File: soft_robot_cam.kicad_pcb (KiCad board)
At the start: 4 copper layers, 134.7 x 96.5 mm, 122 parts, among them J1 Conn_01x24_Socket, J1 Connector, J10 Screw_Terminal_01x02, J2 Conn_01x06, J2 Screw_Terminal_01x02, J3 Conn_01x03, J3 Screw_Terminal_01x02, J4 Conn_01x05_Pin, J6 Screw_Terminal_01x02, J7 Screw_Terminal_01x02, J8 Conn_01x24_Socket, J9 Screw_Terminal_01x02, Q1 S8050, Q2 S8050, Q3 AO3401A, SW1 reset, SW2 SW_DPST_x2, SW4 SW_DIP_x02, U1 DRV8872DDA, U12 XC6206P282MR, U13 XC6206P122MR, U14 SY8113IADC, U2 DRV8872DDA, U3 MPU6500, U4 AP2112K-1.2, U4 DRV8874PWPR, U5 3.3v, U5 DRV8874PWPR, U6 ESP32-WROVER-E, U7 TC2014-2.8VxCTTR, U9 ESP32-S3-WROOM-1-N16R8

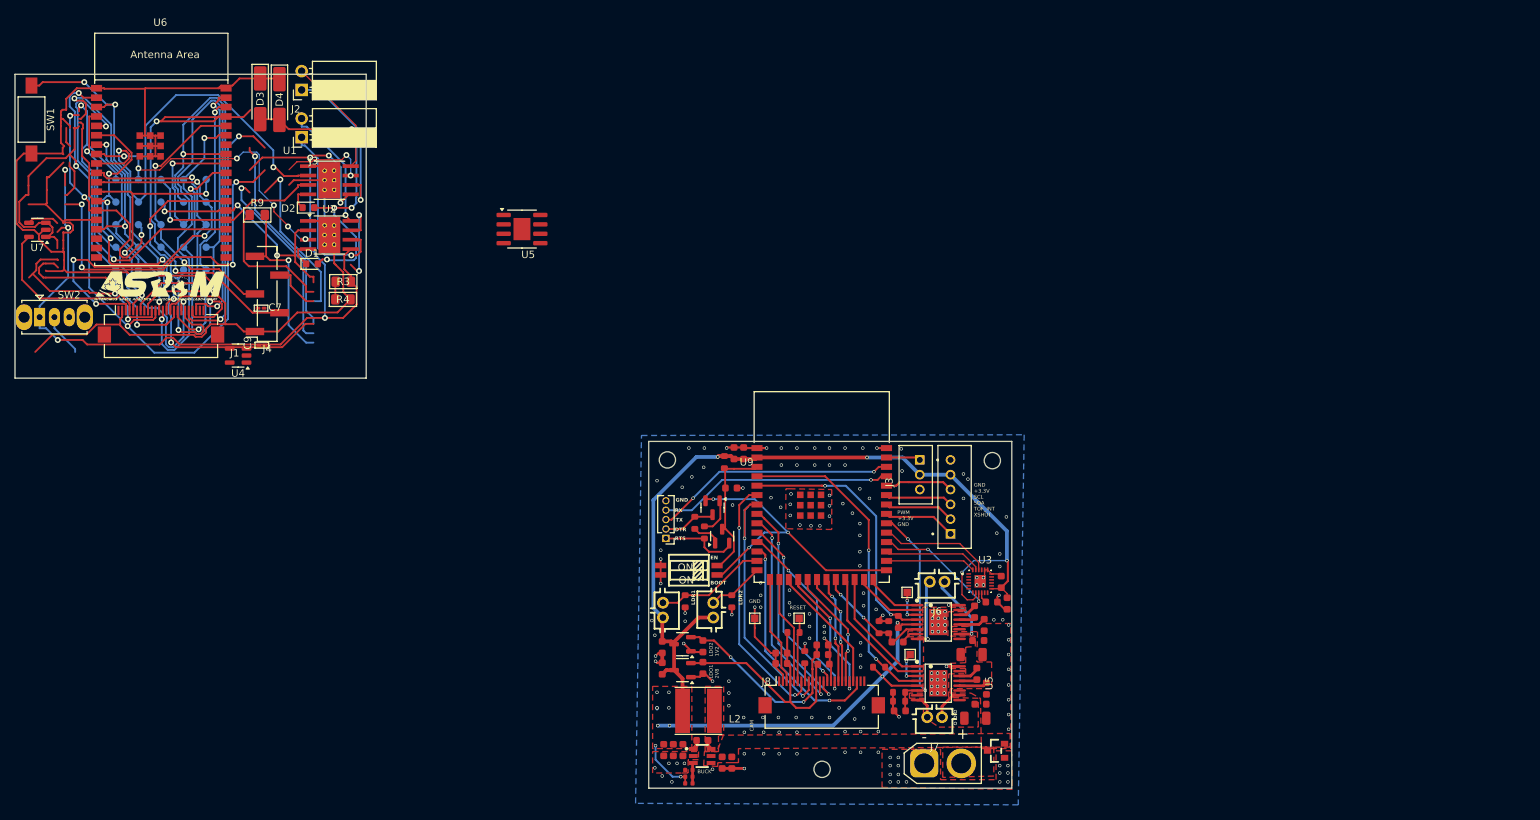
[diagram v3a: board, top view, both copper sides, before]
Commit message: Added most 3D models, revised some layout based off 3D model placement, need to verify JST-XH placement and ensure no design errors.
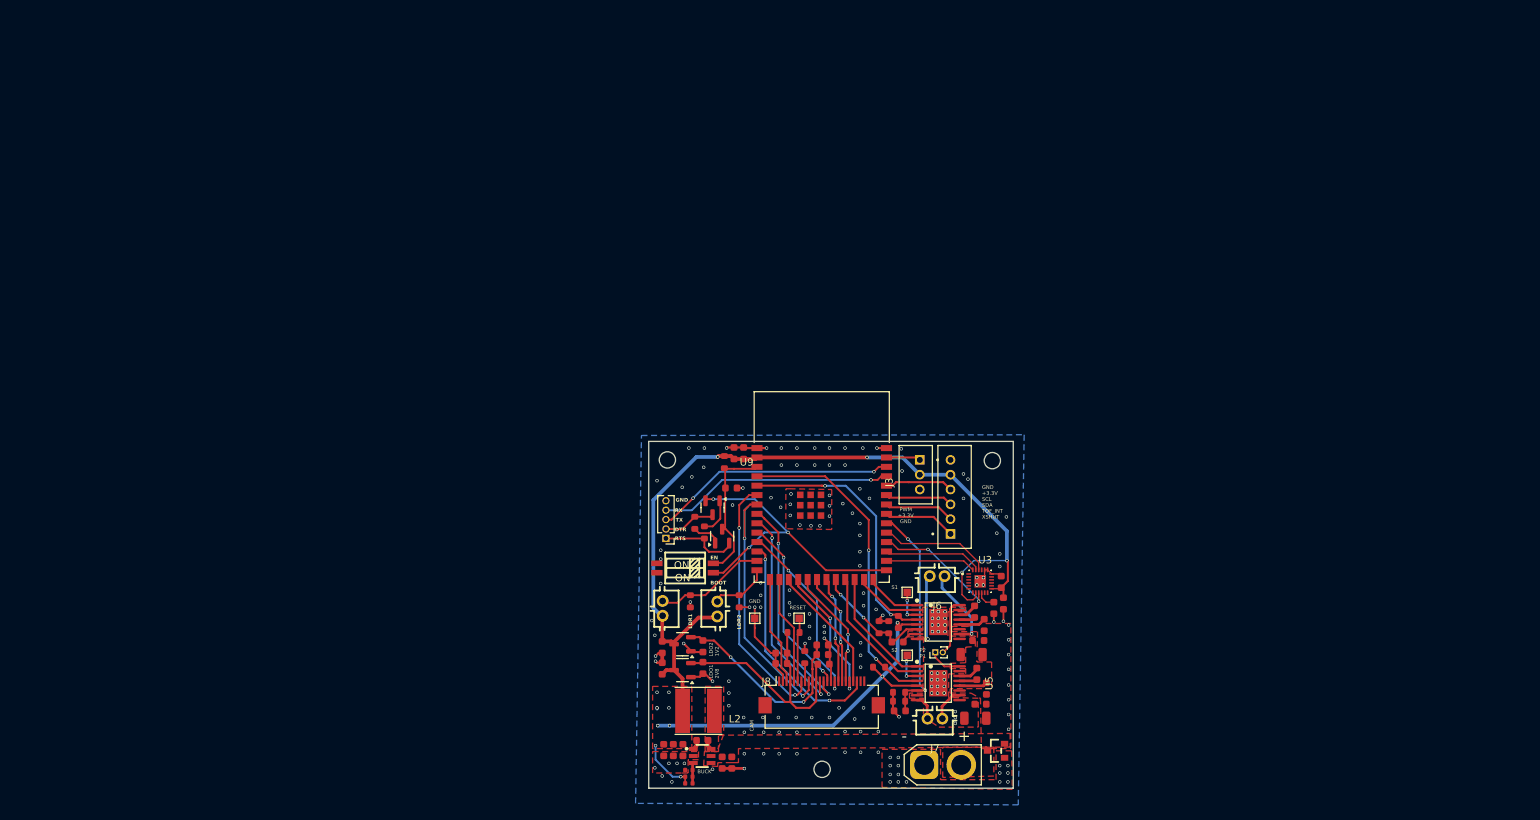
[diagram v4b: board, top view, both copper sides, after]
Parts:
- removed the C7 at (106.1, 97.2)
- removed the C9 at (106.2, 102.2)
- removed D1, D2: LED, LED_SMD:LED_0603_1608Metric
- removed D3, D4: BZV55B3V0, Diode_SMD:D_MiniMELF_Handsoldering
- removed G***: LOGO, LOGO
- removed H1, H10, H11, H12, H13, H14, H15, H16, H17, H18, H19, H2, H20, H21, H22, H23, H24, H25, H3, H4, H5, H6, H7, H8, H9: MountingHole_Pad, TestPoint:TestPoint_Pad_D1.0mm
- removed the J1 at (92.6, 99.4)
- removed the J2 at (111.6, 67.7)
- removed the J3 at (111.6, 74.1)
- removed the J4 at (106.9, 95.3)
- removed R3: 10k, PCM_Resistor_SMD_AKL:R_0805_2012Metric_Pad1.15x1.40mm_HandSolder
- removed R4: 1k, PCM_Resistor_SMD_AKL:R_0805_2012Metric_Pad1.15x1.40mm_HandSolder
- removed the R9 at (105.6, 84.6)
- removed SW1: reset, Button_Switch_SMD:SW_SPST_FSMSM
- removed SW2: SW_DPST_x2, Button_Switch_THT:SW_Slide_SPDT_Straight_CK_OS102011MS2Q
- removed U1, U2: DRV8872DDA, Package_SO:Texas_HTSOP-8-1EP_3.9x4.9mm_P1.27mm_EP2.95x4.9mm_Mask2.4x3.1mm_ThermalVias
- removed the U4 at (103.0, 103.6)
- removed the U5 at (141.4, 86.5)
- removed U6: ESP32-WROVER-E, Espressif:ESP32-WROVER-E
- removed U7: TC2014-2.8VxCTTR, Package_TO_SOT_SMD:SOT-23-5
- added J12: Screw_Terminal_01x02, Connector_PinHeader_1.00mm:PinHeader_1x02_P1.00mm_Vertical, F.Cu at (197.2, 143.7)
- moved R10 1.00 mm to (170.7, 136.8)
- moved C2 0.85 mm to (205.1, 137.7), turned to 90 degrees
- moved J6 0.76 mm to (197.4, 133.4)
- moved R9 0.70 mm to (164.1, 136.8)
- moved SW4 0.58 mm to (163.4, 132.3)
- moved J10 0.56 mm to (167.7, 137.8)
- moved C3 0.50 mm to (206.4, 137.1)
- moved REF** 0.41 mm to (193.4, 144.1)
- moved J9 0.25 mm to (160.4, 137.8)
- moved J7 0.20 mm to (197.1, 152.7)
- moved J1 0.20 mm to (195.7, 158.9)
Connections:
- U4 pad 16: Net-(U4-PMODE) -> /PMODE1
- U5 pad 16: Net-(U5-PMODE) -> /PMODE2
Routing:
- net CAM_AGND: track 234.4 -> 0.00 mm
- net VIN_SW: track 125.2 -> 0.00 mm, vias 7 -> 0
- net 3.3v: track 120.0 -> 0.00 mm, vias 4 -> 0
- net EN: track 99.0 -> 0.00 mm, vias 4 -> 0
- net CAM_D4: track 68.5 -> 0.00 mm, vias 2 -> 0
- net TXD_esp: track 60.7 -> 0.00 mm, vias 2 -> 0
- net CAM_D5: track 59.3 -> 0.00 mm, vias 2 -> 0
- net M1_B: track 55.1 -> 0.00 mm, vias 2 -> 0
- net CAM_SDA: track 54.1 -> 0.00 mm, vias 4 -> 0
- net Net-(U5-EN): track 48.3 -> 0.00 mm, vias 4 -> 0
- net IMU_CS: track 47.5 -> 0.00 mm, vias 2 -> 0
- net CAM_D7: track 46.8 -> 0.00 mm, vias 2 -> 0
- net CAM_D6: track 46.6 -> 0.00 mm, vias 2 -> 0
- net Net-(D1-A): track 42.8 -> 0.00 mm, vias 4 -> 0
- net CAM_MCLK: track 42.3 -> 0.00 mm, vias 2 -> 0
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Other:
- board size 134.7 x 96.5 mm -> 49.2 x 46.9 mm
- board text added: "P2 P1"
- board text added: "PWM +3.3V GND"
- board text added: "S1"
- board text added: "S2"
- board text removed: "+3.3V"
- board text removed: "PWM"

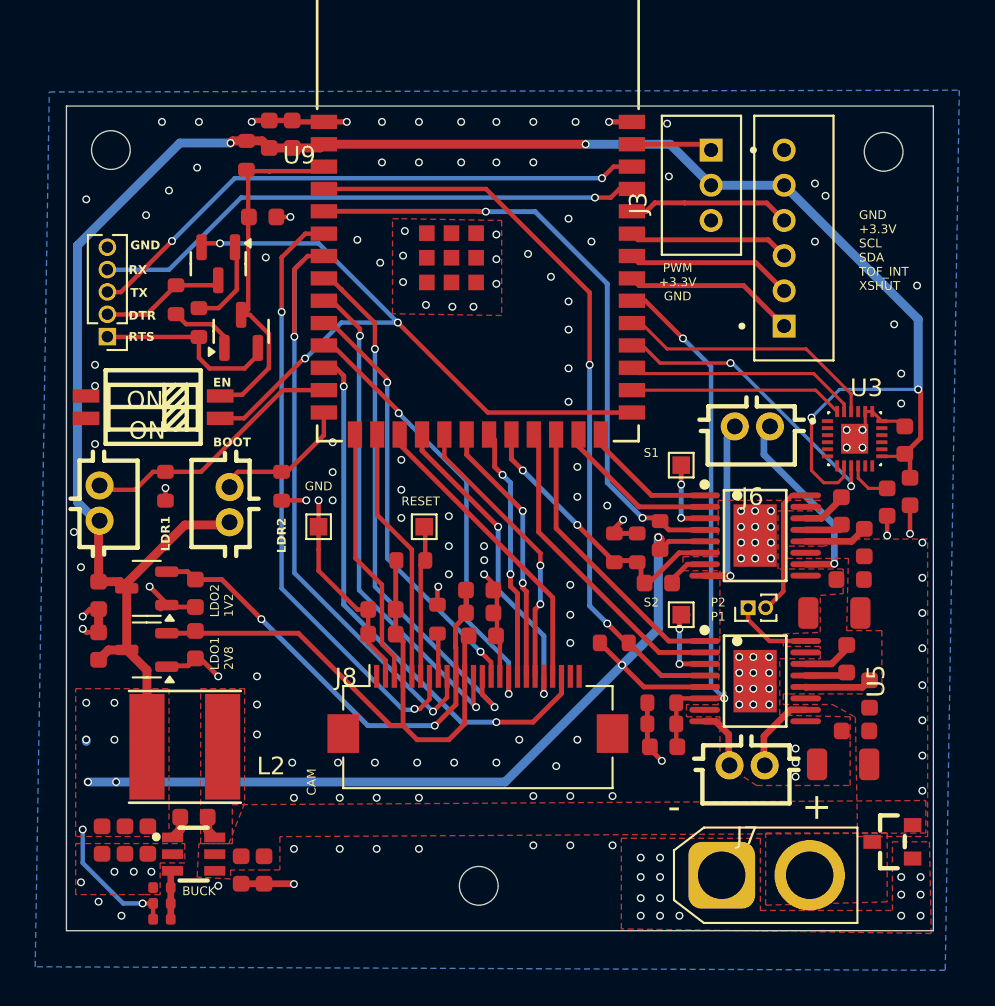
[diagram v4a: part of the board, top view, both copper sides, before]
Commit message: Reviewed connector placement, chaning footprint to ensure clearance, added LEDs on Buck, slightly modified layout to improve spacing and clearance. Next is a full design and BOM review.
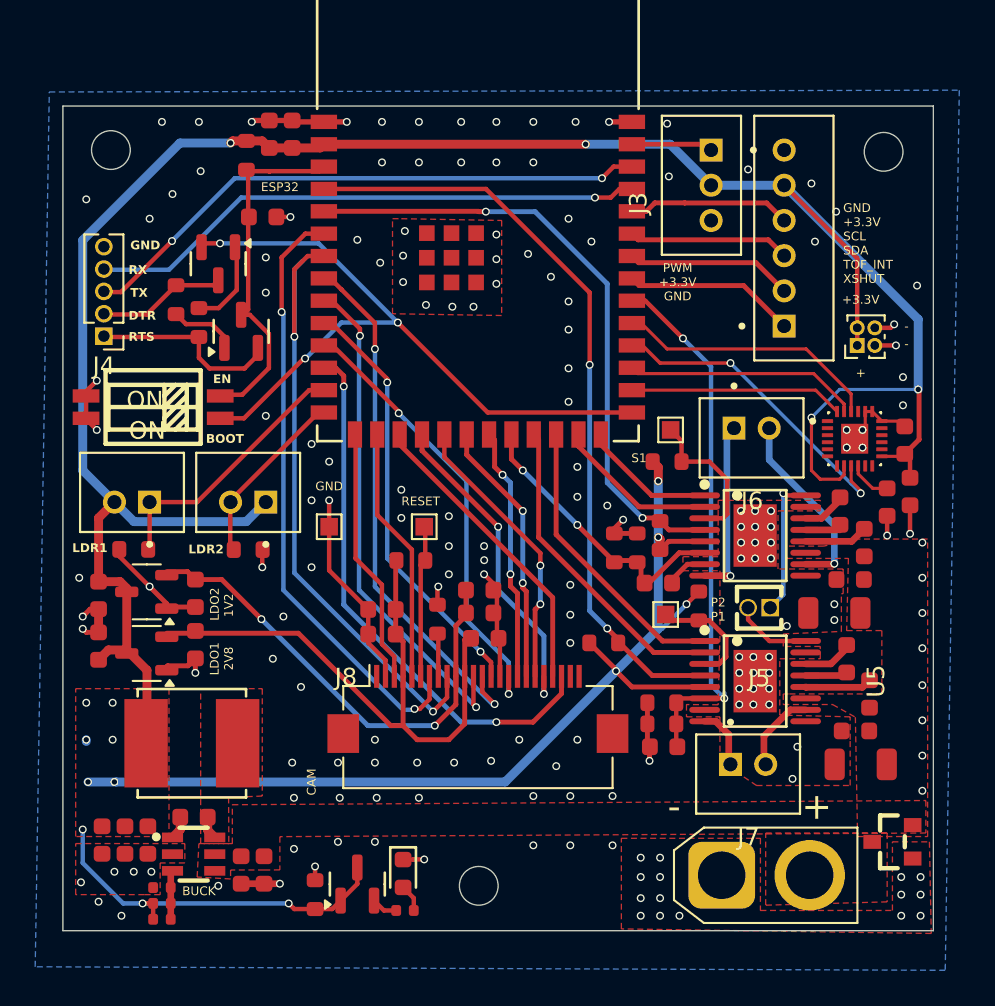
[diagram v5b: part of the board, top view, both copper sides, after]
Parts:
- removed J12: Screw_Terminal_01x02, Connector_PinHeader_1.00mm:PinHeader_1x02_P1.00mm_Vertical
- removed L2: SRN6045-6R8Y, easyeda2kicad:IND-SMD_L6.0-W6.0_SRN6045
- added D2: Red, PCM_JLCPCB:D_0603, F.Cu at (177.6, 158.8)
- added J11: Conn_02x02_Counter_Clockwise, Connector_PinHeader_1.00mm:PinHeader_2x02_P1.00mm_Vertical, F.Cu at (203.4, 128.8)
- added J5: Conn_01x02_Pin, easyeda2kicad:HDR-TH_2P-P1.27-V-M, F.Cu at (197.8, 143.7)
- added L1: SWPA6028S6R8MT, easyeda2kicad:IND-SMD_L6.0-W6.0_SWPA6045S, F.Cu at (165.6, 151.4)
- added Q4: AO3400A, PCM_JLCPCB:Q_SOT-23, F.Cu at (175.0, 159.4)
- added R16: 4.7kΩ, PCM_JLCPCB:R_0603, F.Cu at (192.6, 135.4)
- added R17: 4.7kΩ, PCM_JLCPCB:R_0603, F.Cu at (194.4, 143.6)
- added R22: 10kΩ, PCM_JLCPCB:R_0603, F.Cu at (172.6, 160.0)
- added R4: 200Ω, PCM_JLCPCB:R_0402, F.Cu at (177.7, 160.9)
- J10, J6, J7, J9: footprint easyeda2kicad:CONN-TH_B2B-PH-K-S -> easyeda2kicad:JST_B2B-PH-K-S
- moved R10 4.07 mm to (168.8, 140.4), turned to 0 degrees
- moved R9 4.01 mm to (162.3, 140.4), turned to 0 degrees
- moved REF** 2.09 mm to (192.8, 133.6)
- moved J9 1.94 mm to (162.2, 137.2), turned to 0 degrees
- moved J10 1.27 mm to (168.8, 137.2), turned to 0 degrees
- moved C35 1.00 mm to (203.6, 152.6)
- moved REF** 0.89 mm to (192.5, 144.1)
- moved J6 0.65 mm to (197.4, 134.1)
- moved GND 0.60 mm to (173.4, 139.1)
- moved R21 0.60 mm to (189.0, 145.7)
- moved J7 0.50 mm to (197.2, 153.2)
- moved J4 0.20 mm to (160.6, 128.3)
- moved U12 0.20 mm to (163.0, 146.3)
- moved U13 0.20 mm to (163.0, 142.8)
- moved C25 0.20 mm to (182.2, 145.4)
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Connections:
- net /nSLEEP_A renamed Net-(U4-nSLEEP)
- net /nSLEEP_B renamed Net-(U5-nSLEEP)
- J10 pad 1: /LDR2 -> +3.3V
- J10 pad 2: +3.3V -> /LDR2
- J9 pad 1: +3.3V -> /LDR1
- J9 pad 2: /LDR1 -> +3.3V
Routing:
- net +3.3V: track 177.4 -> 213.0 mm, vias 14 -> 17
- net GND: track 57.0 -> 63.8 mm, vias 173 -> 178
- net Net-(U4-nSLEEP): track 4.38 -> 8.43 mm, vias 2 -> 0
- net Net-(U5-nSLEEP): track 4.73 -> 6.46 mm, vias 2 -> 0
- net /LDR2: track 8.47 -> 10.2 mm
- net Net-(D2-Pad2): track 0.00 -> 1.56 mm
- net Net-(Q4-S): track 0.00 -> 1.49 mm
- net /MISO1: track 17.1 -> 18.3 mm
- net /OUT1_A: track 9.55 -> 10.3 mm
- net /PMODE1: track 7.86 -> 8.13 mm, vias 0 -> 1
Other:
- board size 49.2 x 46.9 mm -> 49.4 x 46.9 mm
- board text added: "+"
- board text added: "+3.3V"
- board text added: "-"
- board text added: "LDO1"
- board text removed: "S2"

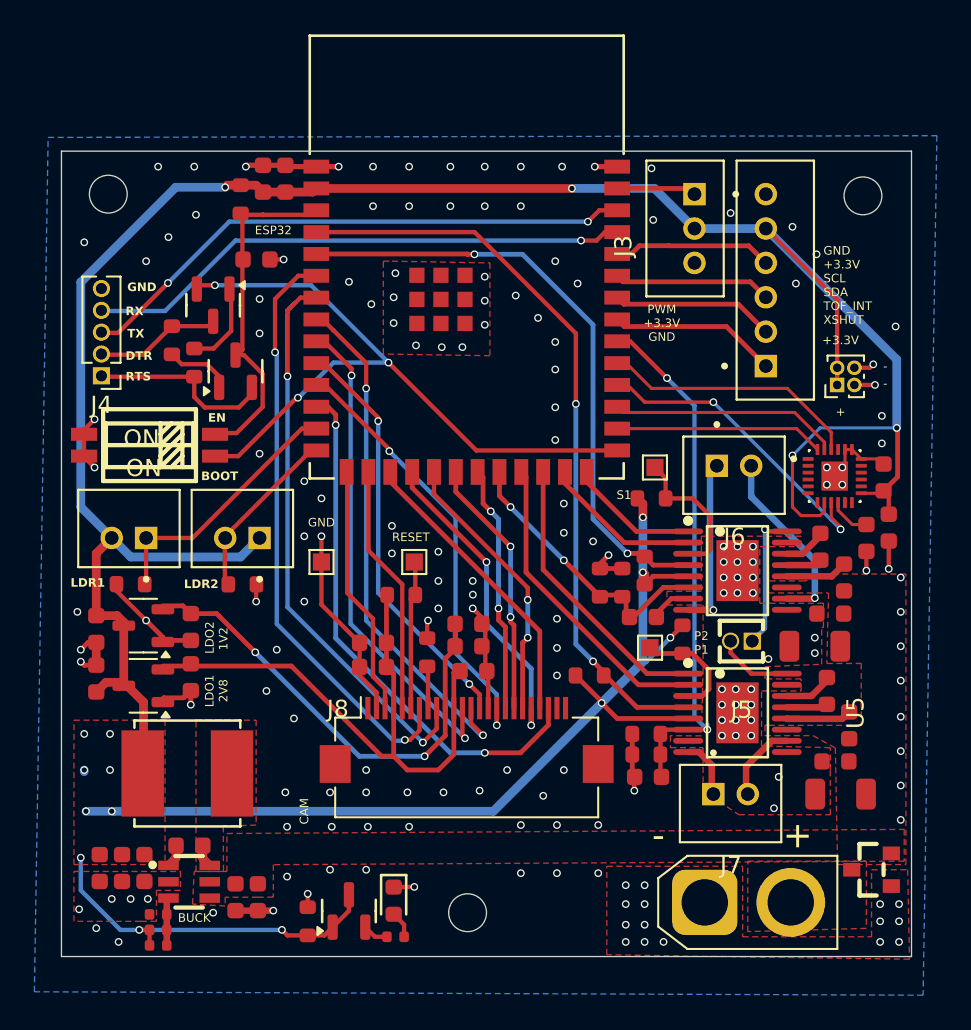
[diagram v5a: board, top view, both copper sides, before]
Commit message: Reviewed and fixed wiring, adding eFuses and protection IC.
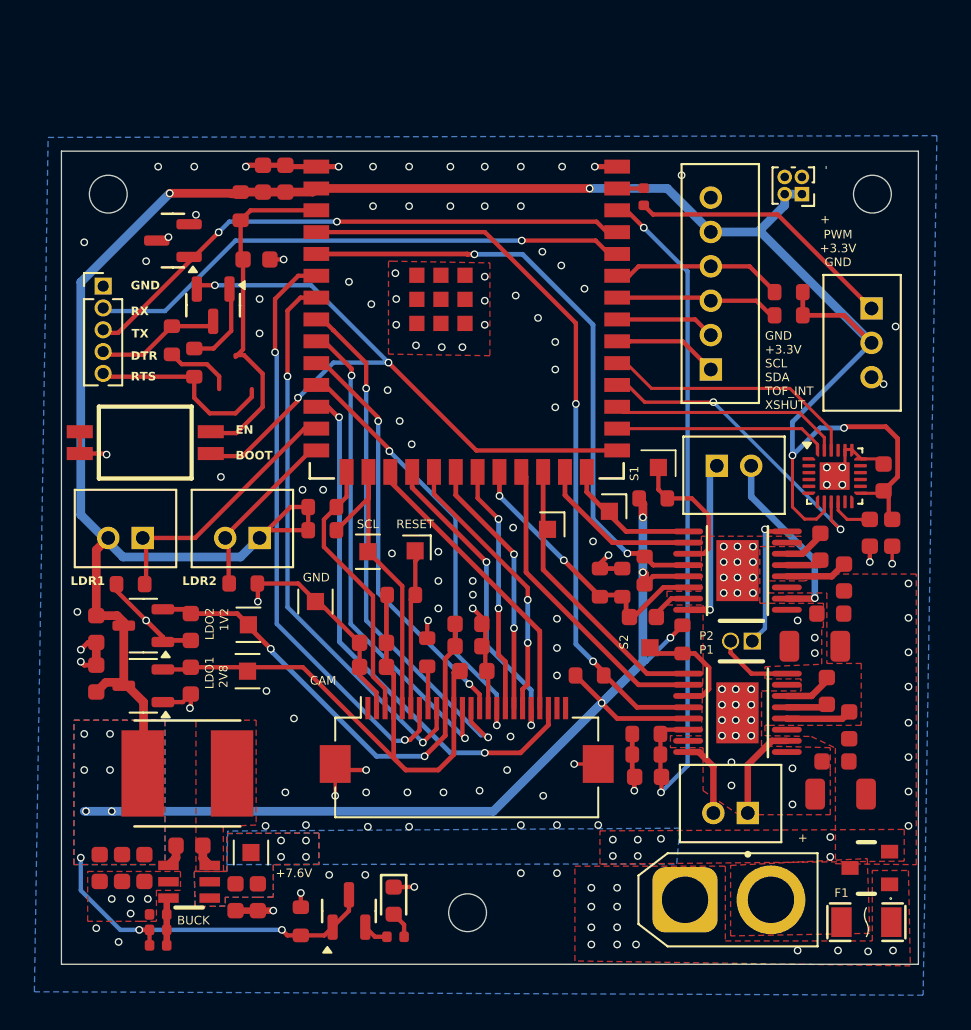
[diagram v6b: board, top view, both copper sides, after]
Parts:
- added +7.6V: TestPoint_Pad_1.0x1.0mm, TestPoint:TestPoint_Pad_1.0x1.0mm, F.Cu at (169.3, 156.0)
- added +7.6V: TestPoint_Pad_1.0x1.0mm, TestPoint:TestPoint_Pad_1.0x1.0mm, F.Cu at (169.2, 142.8)
- added +7.6V: TestPoint_Pad_1.0x1.0mm, TestPoint:TestPoint_Pad_1.0x1.0mm, F.Cu at (169.1, 145.4)
- added F1: JFC1206-1450FS, easyeda2kicad:F1206, F.Cu at (205.1, 160.1)
- added GND: TestPoint_Pad_1.0x1.0mm, TestPoint:TestPoint_Pad_1.0x1.0mm, F.Cu at (186.6, 137.2)
- added GND: TestPoint_Pad_1.0x1.0mm, TestPoint:TestPoint_Pad_1.0x1.0mm, F.Cu at (190.2, 136.2)
- added GND: TestPoint_Pad_1.0x1.0mm, TestPoint:TestPoint_Pad_1.0x1.0mm, F.Cu at (176.1, 138.5)
- added R11: 4.7kΩ, PCM_JLCPCB:R_0603, F.Cu at (200.6, 123.4)
- added R18: 200Ω, PCM_JLCPCB:R_0402, F.Cu at (192.2, 117.8)
- added R23: 4.7kΩ, PCM_JLCPCB:R_0603, F.Cu at (200.6, 124.8)
- added R24: 4.7kΩ, PCM_JLCPCB:R_0603, F.Cu at (173.4, 137.2)
- added R3: 4.7kΩ, PCM_JLCPCB:R_0603, F.Cu at (173.4, 135.9)
- L1: value SWPA6028S6R8MT -> 6.8uH
- U3: footprint easyeda2kicad:QFN40P300X300X95-25N -> Package_DFN_QFN:QFN-24-1EP_3x3mm_P0.4mm_EP1.75x1.6mm
- moved J3 12.3 mm to (204.8, 126.3)
- moved J11 11.3 mm to (201.3, 117.7), turned to 180 degrees
- moved Q1 8.43 mm to (164.8, 120.4), turned to 180 degrees
- moved J4 5.22 mm to (160.7, 123.0), turned to 0 degrees
- moved J2 3.21 mm to (196.6, 122.9)
- moved GND 2.33 mm to (173.1, 141.4)
- moved J1 1.16 mm to (194.6, 158.8)
- moved REF** 0.65 mm to (178.8, 138.4)
- moved REF** 0.56 mm to (205.4, 117.7)
- moved R12 0.40 mm to (168.7, 118.4)
- moved R22 0.40 mm to (172.2, 160.0)
- moved C3 0.36 mm to (206.6, 137.4)
- moved C2 0.36 mm to (205.3, 137.4)
- moved SW4 0.29 mm to (163.2, 132.2)
- moved C17 0.20 mm to (165.8, 146.0)
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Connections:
- J7 pad 1: /OUT1_B -> /OUT2_B
- J7 pad 2: /OUT2_B -> /OUT1_B
- U9 pad 32: /I_SENSE_B -> /XSHUT
- U9 pad 33: /XSHUT -> /TOF_INT
- U9 pad 34: /TOF_INT -> /SDA
- U9 pad 35: /SDA -> /SCL
- U9 pad 36: /SCL -> /RXD0
- U9 pad 37: /RXD0 -> /TXD0
- U9 pad 38: /TXD0 -> /I_SENSE_B
- U9 pad 39: /S_PWM -> Net-(U9-IO1)
- U9 pad 42: (no net) -> GND
- U9 pad 43: (no net) -> GND
- U9 pad 44: (no net) -> GND
- U9 pad 45: (no net) -> GND
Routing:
- net /I_SENSE_B: track 30.5 -> 41.7 mm
- net /S_PWM: track 4.64 -> 15.7 mm
- net +3.3V: track 213.0 -> 222.8 mm
- net /HREF: track 37.2 -> 32.7 mm
- net /I2C_SCL: track 14.6 -> 18.7 mm
- net /TOF_INT: track 9.47 -> 5.98 mm
- net /XSHUT: track 9.77 -> 6.49 mm
- net GND: track 63.8 -> 65.5 mm, vias 178 -> 164
- net Net-(U9-IO1): track 0.00 -> 1.56 mm
- net /OUT1_B: track 3.28 -> 4.52 mm
- net /OUT2_B: track 4.49 -> 5.65 mm
- net /I2C_SDA: track 14.7 -> 15.8 mm
- net /SCL: track 9.26 -> 10.2 mm
- net /XCLK: track 30.4 -> 31.0 mm
- net +7.6V: vias 0 -> 11
- added copper zone on B.Cu, net +3.3V
- added copper zone on B.Cu, net +7.6V
- removed copper zone on In2.Cu, net +7.6V
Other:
- board size 49.4 x 46.9 mm -> 49.8 x 47.3 mm
- board text added: "LDR"
- board text added: "P1"
- board text added: "P2"
- board text added: "S2"
- board text added: "SCL"
